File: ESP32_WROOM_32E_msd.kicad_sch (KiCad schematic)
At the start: 20 parts, among them J1 XH_6pin, J2 XH_6pin, J3 XH_2pin, J4 XH_2pin, SW1 SW_SPDT, U2 MCP2561-E-SN

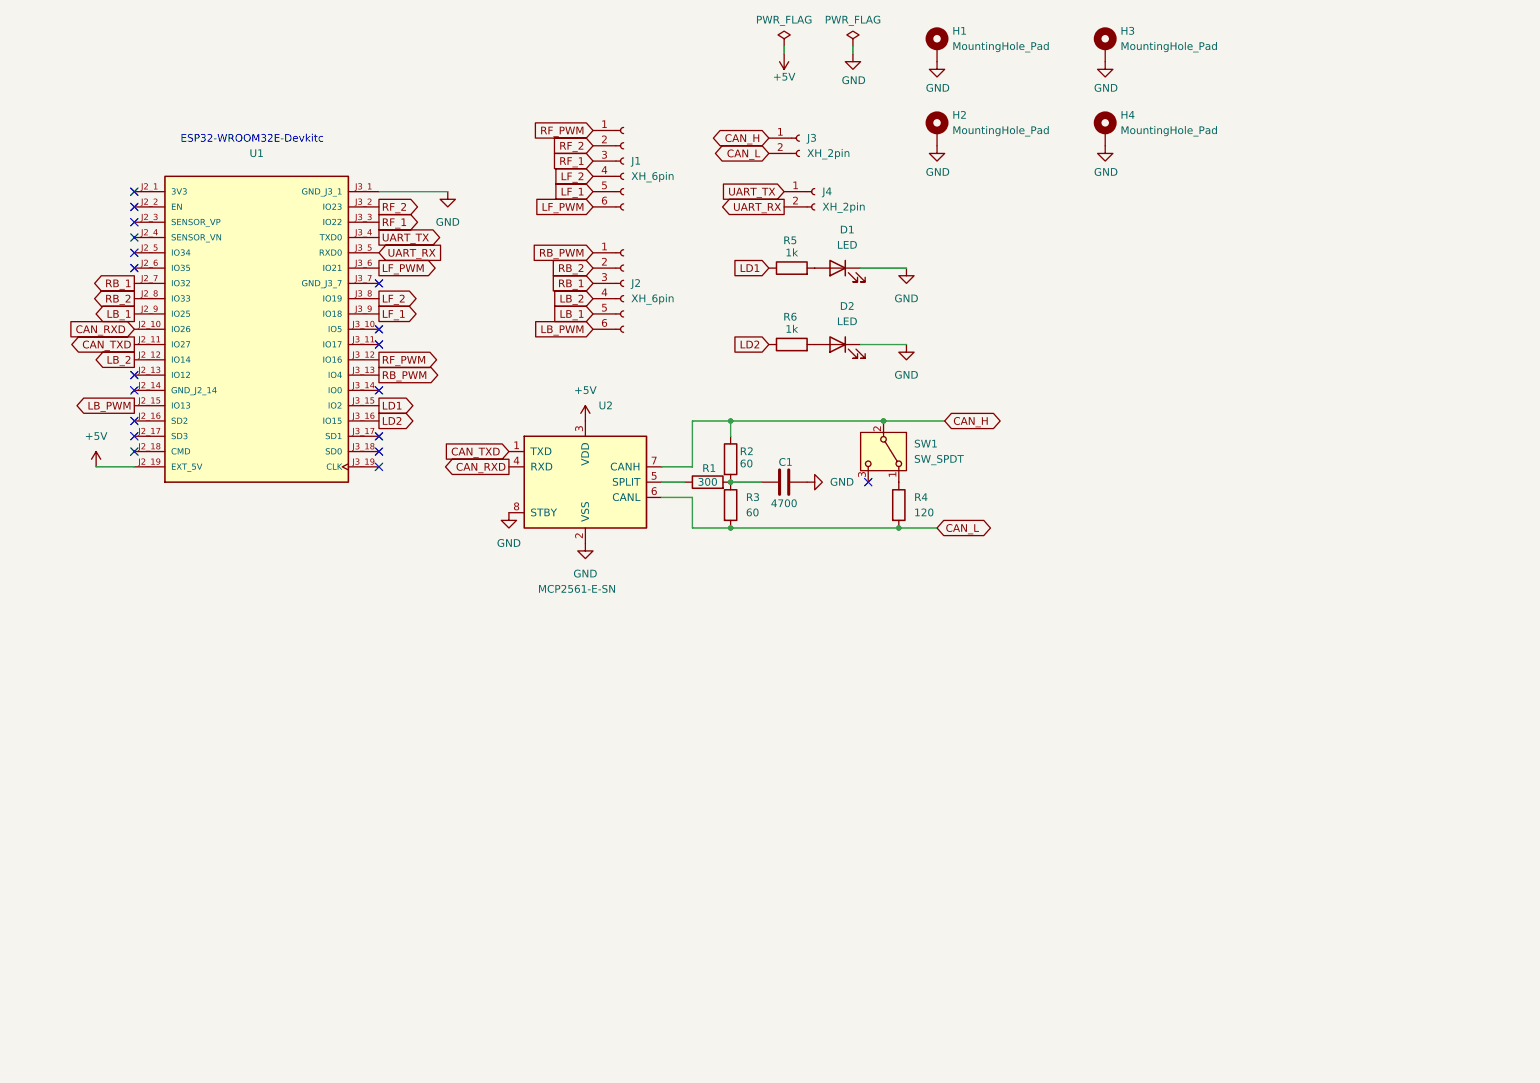
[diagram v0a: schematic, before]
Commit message: change switch
because no stock on JLCPCB
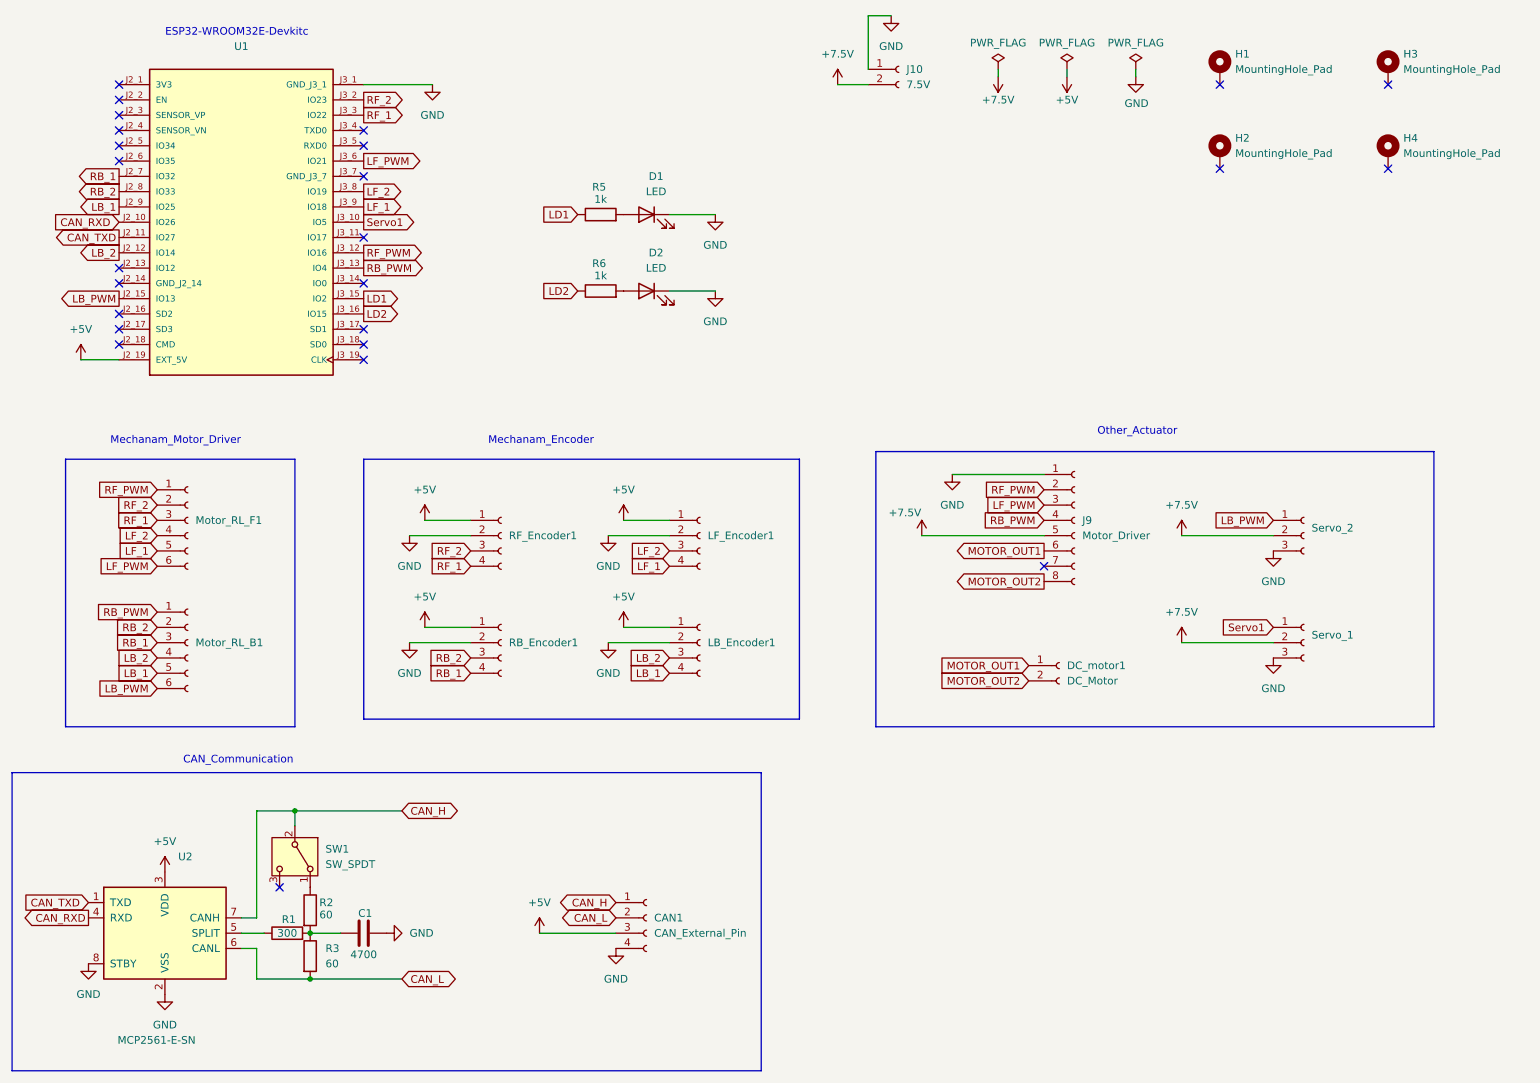
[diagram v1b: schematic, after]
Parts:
- removed J3, J4: XH_2pin, Connector_JST:JST_XH_B2B-XH-A_1x02_P2.50mm_Vertical, symbol Connector:Conn_01x02_Socket
- removed R4: 120, Resistor_SMD:R_0603_1608Metric, symbol Device:R
- added CAN1: CAN_External_Pin, Connector_JST:JST_XH_B4B-XH-A_1x04_P2.50mm_Vertical, symbol Connector:Conn_01x04_Socket
- added DC_motor1: DC_Motor, Connector_JST:JST_XH_B2B-XH-A_1x02_P2.50mm_Vertical, symbol Connector:Conn_01x02_Socket
- added J10: 7.5V, Connector_AMASS:AMASS_XT30PW-F_1x02_P2.50mm_Horizontal, symbol Connector:Conn_01x02_Socket
- added J9: Motor_Driver, Connector_PinHeader_2.54mm:PinHeader_1x08_P2.54mm_Vertical, symbol Connector:Conn_01x08_Socket
- added LB_Encoder1: LB_Encoder, Connector_JST:JST_XH_B4B-XH-A_1x04_P2.50mm_Vertical, symbol Connector:Conn_01x04_Socket
- added LF_Encoder1: LF_Encoder, Connector_JST:JST_XH_B4B-XH-A_1x04_P2.50mm_Vertical, symbol Connector:Conn_01x04_Socket
- added RB_Encoder1: RB_Encoder, Connector_JST:JST_XH_B4B-XH-A_1x04_P2.50mm_Vertical, symbol Connector:Conn_01x04_Socket
- added RF_Encoder1: RF_Encoder, Connector_JST:JST_XH_B4B-XH-A_1x04_P2.50mm_Vertical, symbol Connector:Conn_01x04_Socket
- added Servo_1: Servo_1, Connector_JST:JST_XH_B3B-XH-A_1x03_P2.50mm_Vertical, symbol Connector:Conn_01x03_Socket
- added Servo_2: Servo_2, Connector_JST:JST_XH_B3B-XH-A_1x03_P2.50mm_Vertical, symbol Connector:Conn_01x03_Socket
- Motor_RL_B1: renamed from J2; value XH_6pin -> Motor_RL_B
- Motor_RL_F1: renamed from J1; value XH_6pin -> Motor_RL_F
- SW1: footprint Original:slide_SW -> Connector_PinHeader_2.54mm:PinHeader_1x03_P2.54mm_Vertical
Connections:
- net +5V: now also CAN1.3 (Pin_3), LB_Encoder1.1 (Pin_1), LF_Encoder1.1 (Pin_1), RB_Encoder1.1 (Pin_1), RF_Encoder1.1 (Pin_1)
- net CAN_H: now also CAN1.1 (Pin_1); no longer R2.1
- net CAN_L: now also CAN1.2 (Pin_2)
- net GND: now also CAN1.4 (Pin_4), J10.1 (Pin_1), J9.1 (Pin_1), LB_Encoder1.2 (Pin_2), LF_Encoder1.2 (Pin_2), RB_Encoder1.2 (Pin_2), RF_Encoder1.2 (Pin_2), Servo_1.3 (Pin_3), Servo_2.3 (Pin_3); no longer H1.1, H2.1, H3.1, H4.1
- net LB_1: now also LB_Encoder1.4 (Pin_4)
- net LB_2: now also LB_Encoder1.3 (Pin_3)
- net LB_PWM: now also Servo_2.1 (Pin_1)
- net LF_1: now also LF_Encoder1.4 (Pin_4)
- net LF_2: now also LF_Encoder1.3 (Pin_3)
- net LF_PWM: now also J9.3 (Pin_3)
- net RB_1: now also RB_Encoder1.4 (Pin_4)
- net RB_2: now also RB_Encoder1.3 (Pin_3)
- net RB_PWM: now also J9.4 (Pin_4)
- net RF_1: now also RF_Encoder1.4 (Pin_4)
- net RF_2: now also RF_Encoder1.3 (Pin_3)
- net RF_PWM: now also J9.2 (Pin_2)
- net at SW1.1 (A): now also R2.1
- net Servo1: now reaches U1.J3_10 (IO5)
- net Servo1: now also Servo_1.1 (Pin_1)
- net UART_RX: no longer names the net of U1.J3_5 (RXD0)
- net UART_TX: no longer names the net of U1.J3_4 (TXD0)
- new net +7.5V: J10.2 (Pin_2), J9.5 (Pin_5), Servo_1.2 (Pin_2), Servo_2.2 (Pin_2)
- new net MOTOR_OUT1: DC_motor1.1 (Pin_1), J9.6 (Pin_6)
- new net MOTOR_OUT2: DC_motor1.2 (Pin_2), J9.8 (Pin_8)
- no-connect marks 19 -> 25
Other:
- note added: "CAN_Communication"
- note added: "Mechanam_Encoder"
- note added: "Mechanam_Motor_Driver"
- note added: "Other_Actuator"
- moved on the sheet: C1, D1, D2, H1, H2, H3, H4, Motor_RL_B1, Motor_RL_F1, R1, R2, R3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
